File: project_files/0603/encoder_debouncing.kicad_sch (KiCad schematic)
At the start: 18 parts, among them J1 Header, J2 Header, SW1 RotaryEncoder_Switch, U1 74HC14

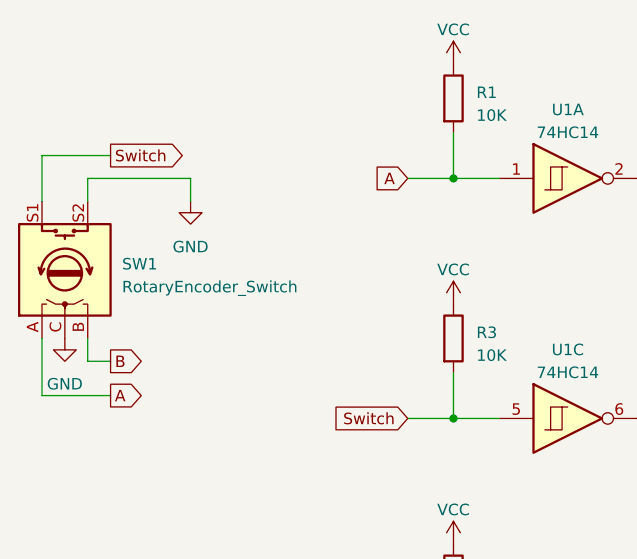
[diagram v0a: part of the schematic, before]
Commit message: added variation with 0805 components
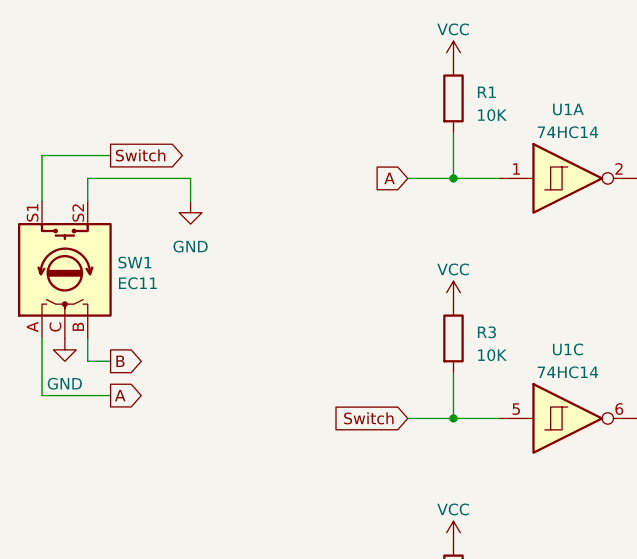
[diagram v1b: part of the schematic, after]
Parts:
- SW1: value RotaryEncoder_Switch -> EC11
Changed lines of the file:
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@@
   (symbol (lib_id "Device:RotaryEncoder_Switch") (at 43.18 66.04 90) (unit 1)
     (in_bom yes) (on_board yes) (fields_autoplaced)
-    (property "Reference" "SW1" (id 0) (at 49.53 65.4049 90)
+    (property "Reference" "SW1" (id 0) (at 49.0221 65.2791 90)
       (effects (font (size 1.27 1.27)) (justify right))
     )
-    (property "Value" "RotaryEncoder_Switch" (id 1) (at 49.53 67.9449 90)
+    (property "Value" "EC11" (id 1) (at 49.0221 67.5778 90)
       (effects (font (size 1.27 1.27)) (justify right))
     )
@@
     )
     (path "/b5f62f87-5584-413e-b908-068a59646f4c"
-      (reference "SW1") (unit 1) (value "RotaryEncoder_Switch") (footprint "Rotary_Encoder:RotaryEncoder_Alps_EC11E-Switch_Vertical_H20mm")
+      (reference "SW1") (unit 1) (value "EC11") (footprint "Rotary_Encoder:RotaryEncoder_Alps_EC11E-Switch_Vertical_H20mm")
     )
     (path "/9ef1eca2-35f4-462a-bf5a-1219784aabb0"
